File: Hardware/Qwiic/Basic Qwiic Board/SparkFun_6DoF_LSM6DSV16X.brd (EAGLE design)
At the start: 25.4 x 25.4 mm, 68 parts, among them J1 QWIIC_RIGHT_ANGLE, J2 QWIIC_RIGHT_ANGLE, U2 LSM6DSV16X

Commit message: Some small adjustments to parts
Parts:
- added U$12, U$21: (no value), top:LSM6DSV16X37
- moved R5 0.23 mm to (17.3, 14.6)
- moved ADDR 0.16 mm to (17.3, 12.7)
- moved U$31 0.15 mm to (5.69, 12.7)
- moved R6 0.13 mm to (17.3, 9.14)
- moved I2C_PU 0.10 mm to (12.7, 10.0)
- moved LOGO3 0.09 mm to (4.12, 12.7)
- moved C4 0.09 mm to (12.7, 15.2)
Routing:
- net SDA/PICO: track 36.8 -> 40.1 mm
- net SCL: track 40.4 -> 43.3 mm
- net GND: track 2.62 -> 2.56 mm, vias 24 -> 22

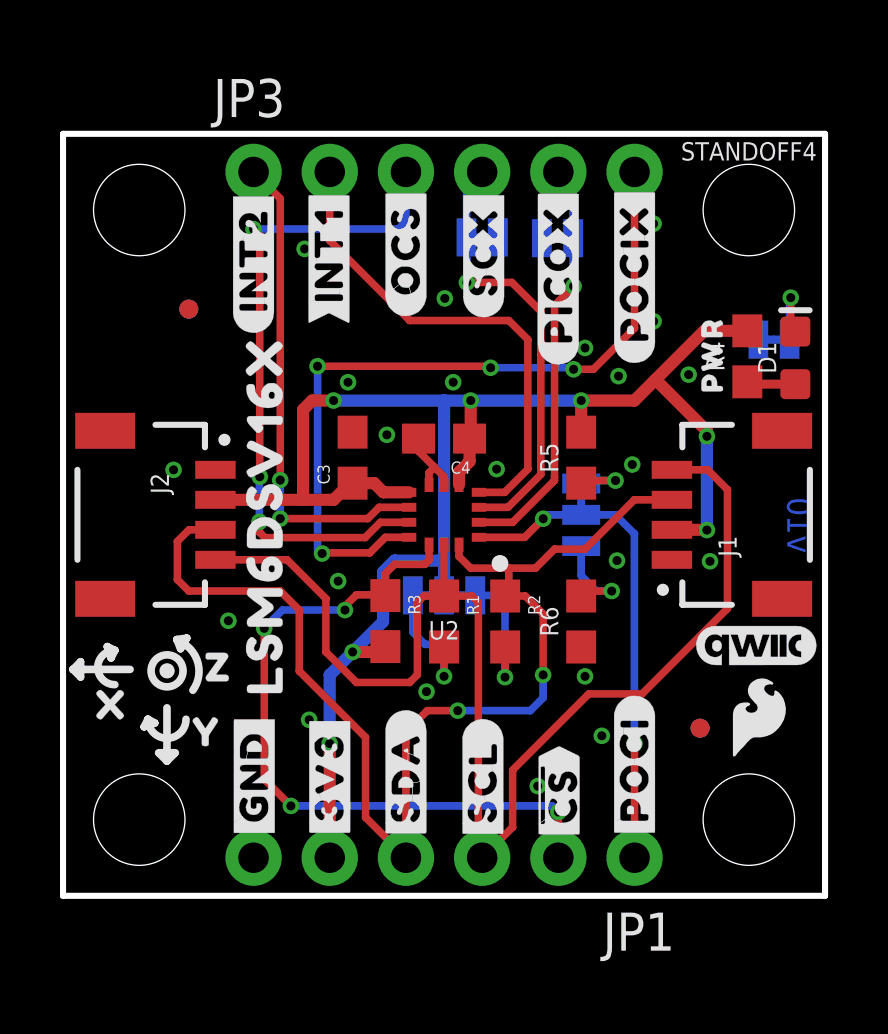
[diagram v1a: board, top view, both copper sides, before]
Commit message: Changes silk label on bottom to "SDX instead of "PICOX"
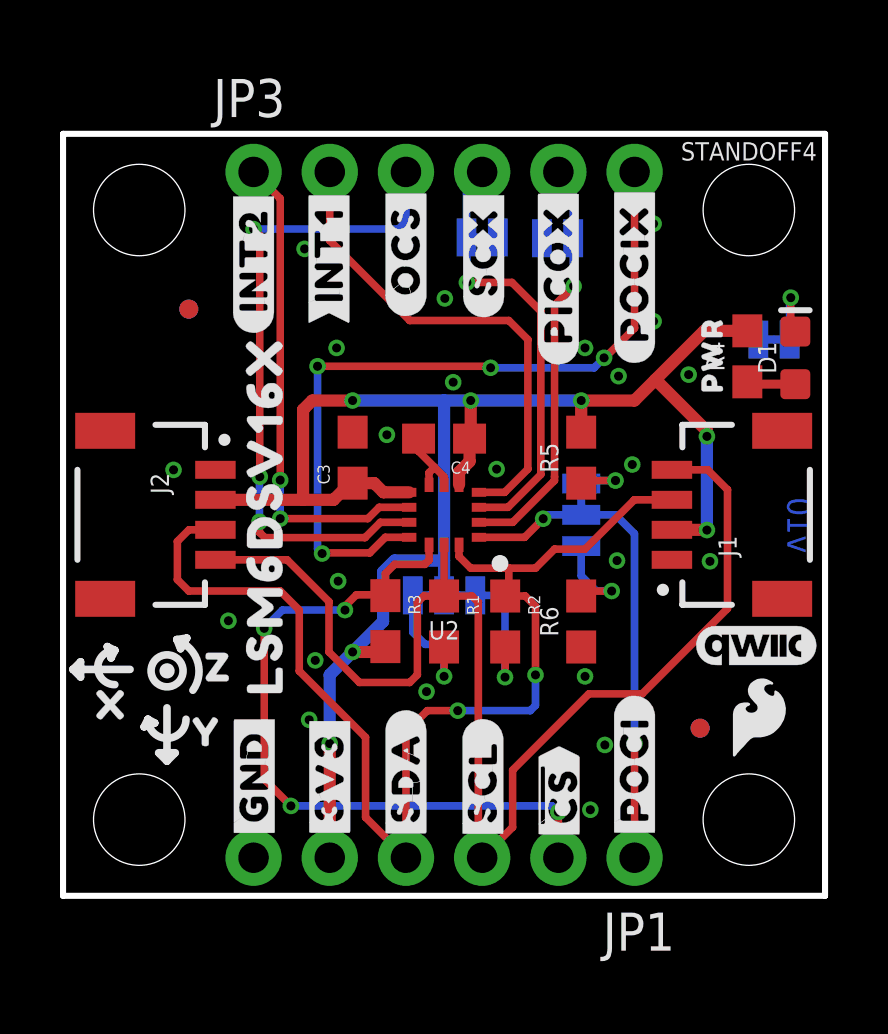
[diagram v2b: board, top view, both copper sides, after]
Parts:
- removed U$32: (no value), ISMTop:#PICOX#9
- added U$30: (no value), bot:#SDX#28
- moved U$14 0.40 mm to (14.7, 13.7)
- moved U$13 0.28 mm to (14.6, 11.9)
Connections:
- net PICO_AUX renamed SDX/PICO_AUX
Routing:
- net GND: vias 22 -> 23
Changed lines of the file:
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@@
 <setting verticaltext="up"/>
 </settings>
-<grid distance="0.05" unitdist="inch" unit="inch" style="dots" multiple="1" display="yes" altdistance="0.005" altunitdist="inch" altunit="inch"/>
+<grid distance="0.05" unitdist="inch" unit="inch" style="dots" multiple="1" display="yes" altdistance="0.001" altunitdist="inch" altunit="inch"/>
 <layers>
 <layer number="1" name="Top" color="4" fill="1" visible="yes" active="yes"/>
@@
 </element>
 <element name="U$16" library="bot" package="#LED#11" value="" x="23.622" y="16.9926" smashed="yes" rot="MR0"/>
-<element name="U$13" library="bot" package="#0X6A#11" value="" x="14.732" y="12.1158" smashed="yes" rot="MR0"/>
-<element name="U$14" library="bot" package="#0X6B#11" value="" x="14.8082" y="13.2842" smashed="yes" rot="MR0"/>
+<element name="U$13" library="bot" package="#0X6A#11" value="" x="14.605" y="11.8618" smashed="yes" rot="MR0"/>
+<element name="U$14" library="bot" package="#0X6B#11" value="" x="14.6812" y="13.6652" smashed="yes" rot="MR0"/>
 <element name="U$25" library="bot" package="#I2C#11" value="" x="12.827" y="8.4582" smashed="yes" rot="MR0"/>
 <element name="U$28" library="top" package="PWR8" value="" x="21.6408" y="18.034" smashed="yes" rot="R90"/>
@@
 <element name="U$11" library="ISMTop" package="#PICOX#10" value="" x="16.51" y="20.7264" smashed="yes" rot="R90"/>
 <element name="U$24" library="ISMTop" package="#POCIX#8" value="" x="19.05" y="20.7772" smashed="yes" rot="R90"/>
-<element name="U$32" library="ISMTop" package="#PICOX#9" value="" x="16.4592" y="18.2372" smashed="yes" rot="MR270"/>
 <element name="U$33" library="ISMTop" package="#POCIX#7" value="" x="19.05" y="20.7772" smashed="yes" rot="MR270"/>
 <element name="U$26" library="ISMTop" package="#PICO#13" value="" x="11.43" y="4.1656" smashed="yes" rot="MR270"/>
@@
 <element name="U$12" library="top" package="LSM6DSV16X37" value="" x="6.731" y="12.7" smashed="yes" rot="R90"/>
 <element name="U$21" library="top" package="LSM6DSV16X37" value="" x="7.239" y="12.7" smashed="yes" rot="MR270"/>
+<element name="U$30" library="bot" package="#SDX#28" value="" x="16.51" y="19.05" smashed="yes" rot="MR270"/>
 </elements>
 <signals>
@@
 <via x="17.399" y="7.3152" extent="1-16" drill="0.3"/>
 <via x="10.795" y="15.367" extent="1-16" drill="0.3"/>
-<via x="9.4996" y="17.1196" extent="1-16" drill="0.3"/>
+<via x="9.1186" y="18.2626" extent="1-16" drill="0.3"/>
 <via x="13.0048" y="17.1196" extent="1-16" drill="0.3"/>
 <via x="17.399" y="18.2626" extent="1-16" drill="0.3"/>
@@
 <via x="18.5166" y="17.3228" extent="1-16" drill="0.3"/>
 <via x="18.9738" y="14.3764" extent="1-16" drill="0.3"/>
-<via x="15.8242" y="3.6576" extent="1-16" drill="0.3"/>
-<via x="17.9578" y="5.334" extent="1-16" drill="0.3"/>
+<via x="17.5768" y="2.8702" extent="1-16" drill="0.3"/>
+<via x="18.0594" y="5.0292" extent="1-16" drill="0.3"/>
 <via x="20.8534" y="17.3736" extent="1-16" drill="0.3"/>
 <via x="21.5646" y="11.1506" extent="1-16" drill="0.3"/>
@@
 <wire x1="12.3825" y1="14.2875" x2="11.85" y2="14.82" width="0.254" layer="1"/>
 <wire x1="11.85" y1="14.82" x2="11.85" y2="15.24" width="0.254" layer="1"/>
+<via x="8.4074" y="7.8486" extent="1-16" drill="0.3"/>
 </signal>
 <signal name="SCL">
@@
 <wire x1="11.811" y1="9.779" x2="11.811" y2="7.366" width="0.254" layer="1"/>
 <wire x1="11.811" y1="7.366" x2="11.557" y2="7.112" width="0.254" layer="1"/>
-<wire x1="8.763" y1="8.128" x2="8.763" y2="9.906" width="0.254" layer="1"/>
+<wire x1="8.8646" y1="8.128" x2="8.8646" y2="9.8044" width="0.254" layer="1"/>
 <wire x1="7.469" y1="11.2" x2="5.08" y2="11.2" width="0.254" layer="1"/>
-<wire x1="11.557" y1="7.112" x2="9.779" y2="7.112" width="0.254" layer="1"/>
-<wire x1="8.763" y1="9.906" x2="7.469" y2="11.2" width="0.254" layer="1"/>
-<wire x1="9.779" y1="7.112" x2="8.763" y2="8.128" width="0.254" layer="1"/>
+<wire x1="11.557" y1="7.112" x2="9.8806" y2="7.112" width="0.254" layer="1"/>
+<wire x1="8.8646" y1="9.8044" x2="7.469" y2="11.2" width="0.254" layer="1"/>
+<wire x1="9.8806" y1="7.112" x2="8.8646" y2="8.128" width="0.254" layer="1"/>
 <wire x1="13.628" y1="9.994" x2="13.843" y2="9.779" width="0.254" layer="1"/>
 <wire x1="19.304" y1="6.731" x2="22.1488" y2="9.5758" width="0.254" layer="1"/>
@@
 <wire x1="15.406" y1="9.994" x2="14.73835" y2="9.994" width="0.254" layer="1"/>
 <wire x1="7.874" y1="9.525" x2="7.874" y2="7.493" width="0.254" layer="1"/>
-<wire x1="16.002" y1="9.398" x2="15.406" y2="9.994" width="0.254" layer="1"/>
-<via x="16.002" y="7.3636" extent="1-16" drill="0.3"/>
+<wire x1="15.748" y1="9.652" x2="15.406" y2="9.994" width="0.254" layer="1"/>
+<via x="15.748" y="7.3636" extent="1-16" drill="0.3"/>
 <wire x1="7.874" y1="7.493" x2="10.0838" y2="5.2832" width="0.254" layer="1"/>
-<wire x1="16.002" y1="6.6016" x2="16.002" y2="7.3636" width="0.254" layer="16"/>
-<wire x1="15.5726" y1="6.1722" x2="16.002" y2="6.6016" width="0.254" layer="16"/>
-<wire x1="16.002" y1="7.3636" x2="16.002" y2="9.398" width="0.254" layer="1"/>
+<wire x1="15.748" y1="6.3476" x2="15.748" y2="7.3636" width="0.254" layer="16"/>
+<wire x1="15.5726" y1="6.1722" x2="15.748" y2="6.3476" width="0.254" layer="16"/>
+<wire x1="15.748" y1="7.3636" x2="15.748" y2="9.652" width="0.254" layer="1"/>
 <wire x1="13.589" y1="10.922" x2="13.2" y2="11.311" width="0.254" layer="1"/>
 <wire x1="13.589" y1="10.922" x2="14.859" y2="10.922" width="0.254" layer="1"/>
@@
 <wire x1="13.8625" y1="11.95" x2="15.3846375" y2="11.95" width="0.254" layer="1"/>
 </signal>
-<signal name="PICO_AUX">
+<signal name="SDX/PICO_AUX">
 <contactref element="JP3" pad="5"/>
 <contactref element="SDX" pad="2"/>
@@
 <wire x1="19.7485" y1="17.2085" x2="21.3732" y2="18.8332" width="0.4064" layer="1"/>
 <wire x1="13.589" y1="16.51" x2="12.7" y2="16.51" width="0.4064" layer="16"/>
-<via x="9.017" y="16.51" extent="1-16" drill="0.3"/>
-<wire x1="9.017" y1="16.51" x2="12.7" y2="16.51" width="0.4064" layer="16"/>
-<wire x1="9.017" y1="16.51" x2="8.3058" y2="16.51" width="0.4064" layer="1"/>
+<via x="9.652" y="16.51" extent="1-16" drill="0.3"/>
+<wire x1="9.652" y1="16.51" x2="12.7" y2="16.51" width="0.4064" layer="16"/>
+<wire x1="9.652" y1="16.51" x2="8.3058" y2="16.51" width="0.4064" layer="1"/>
 <wire x1="8.3058" y1="16.51" x2="8.001" y2="16.2052" width="0.4064" layer="1"/>
 <wire x1="8.001" y1="16.2052" x2="8.001" y2="13.2" width="0.4064" layer="1"/>
@@
 <wire x1="14.201" y1="17.653" x2="8.4836" y2="17.653" width="0.254" layer="1"/>
 <via x="14.2518" y="17.6022" extent="1-16" drill="0.3"/>
-<wire x1="16.9672" y1="17.6022" x2="17.018" y2="17.5514" width="0.254" layer="16"/>
-<wire x1="16.9672" y1="17.6022" x2="14.2518" y2="17.6022" width="0.254" layer="16"/>
-<via x="17.018" y="17.5514" extent="1-16" drill="0.3"/>
-<wire x1="17.018" y1="17.5514" x2="17.6784" y2="17.5514" width="0.254" layer="1"/>
+<wire x1="17.7038" y1="17.6022" x2="18.034" y2="17.9324" width="0.254" layer="16"/>
+<wire x1="17.7038" y1="17.6022" x2="14.2518" y2="17.6022" width="0.254" layer="16"/>
+<via x="18.034" y="17.9324" extent="1-16" drill="0.3"/>
+<wire x1="18.034" y1="17.9324" x2="18.0594" y2="17.9324" width="0.254" layer="1"/>
 <wire x1="19.05" y1="18.923" x2="19.05" y2="24.13" width="0.254" layer="1"/>
-<wire x1="17.6784" y1="17.5514" x2="19.05" y2="18.923" width="0.254" layer="1"/>
+<wire x1="18.0594" y1="17.9324" x2="19.05" y2="18.923" width="0.254" layer="1"/>
 <contactref element="U2" pad="P11"/>
 <wire x1="10.7416375" y1="11.95" x2="11.5375" y2="11.95" width="0.254" layer="1"/>
